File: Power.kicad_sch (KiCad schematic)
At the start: 31 parts, among them J1 Conn_01x02, J6 Conn_01x02, U1 NPM1300-QEAA-R7, U2 TPS76201

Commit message: VSET1 & Ref1 updated
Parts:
- R1: value 270K -> 47K
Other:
- note added: "1) CC1 & CC2 not used. So it is connected to Gnd as mentioned in 6.1.3 USB port detection at page 20&21 in Ref.1 2) Battery NTC not used. So it is connected to ground through 10K resistor 3) To make VOUT1 = 1.8V, VSET1 connected to Resistor K as mentioned in "Table 18: Default VOUT1 using an external resistor" at page 47 Ref.1 4) To make VOUT2 = 3.3V, VSET2 connected to Resistor 100K as mentioned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"
- note removed: "1) CC1 & CC2 not used. So it is connected to Gnd as mentioned in 6.1.3 USB port detection at page 20&21 in Ref.1 2) Battery NTC not used. So it is connected to ground through 10K resistor 3) To make VOUT1 = 2.7V, VSET1 connected to Resistor 270K as mentioned in "Table 18: Default VOUT1 using an external resistor" at page 47 Ref.1 4) To make VOUT2 = 3.3V, VSET2 connected to Resistor 100K as mentio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"
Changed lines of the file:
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@@
 			)
 			(justify left)
+			(href "https://download.mikroe.com/documents/datasheets/nPM1300_datasheet.pdf")
 		)
 	)
@@
 		)
 	)
-	(text "1) CC1 & CC2 not used. So it is connected to Gnd as mentioned in 6.1.3 USB port detection at page 20&21 in Ref.1\n\n2) Battery NTC not used. So it is connected to ground through 10K resistor\n\n3) To make VOUT1 = 2.7V, VSET1 connected to Resistor 270K as mentioned in \"Table 18: Default VOUT1 using an external resistor\" at page 47 Ref.1\n\n4) To make VOUT2 = 3.3V, VSET2 connected to Resistor 100K as mentioned in \"Table 19: Default VOUT2 using an external resistor\" at page 47 Ref.1\n"
+	(text "1) CC1 & CC2 not used. So it is connected to Gnd as mentioned in 6.1.3 USB port detection at page 20&21 in Ref.1\n\n2) Battery NTC not used. So it is connected to ground through 10K resistor\n\n3) To make VOUT1 = 1.8V, VSET1 connected to Resistor K as mentioned in \"Table 18: Default VOUT1 using an external resistor\" at page 47 Ref.1\n\n4) To make VOUT2 = 3.3V, VSET2 connected to Resistor 100K as mentioned in \"Table 19: Default VOUT2 using an external resistor\" at page 47 Ref.1\n"
 		(exclude_from_sim no)
 		(at 14.732 161.29 0)
@@
 			)
 		)
-		(property "Value" "270K"
+		(property "Value" "47K"
 			(at 46.99 105.4099 0)
 			(effects

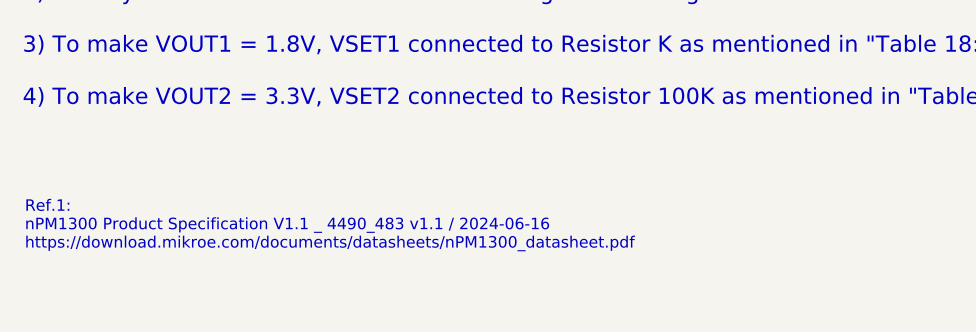
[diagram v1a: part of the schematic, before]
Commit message: Ref link added & Removed charge pumps
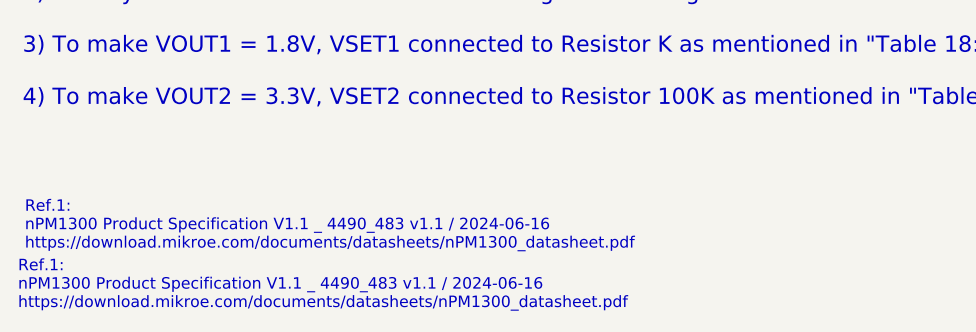
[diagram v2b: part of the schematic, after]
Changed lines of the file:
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@@
 		(comment 2 "K.S.Rangasamy College of Technology")
+	)
+	(text "Ref.1:\nnPM1300 Product Specification V1.1 _ 4490_483 v1.1 / 2024-06-16\nhttps://download.mikroe.com/documents/datasheets/nPM1300_datasheet.pdf"
+		(exclude_from_sim no)
+		(at 14.224 190.754 0)
+		(effects
+			(font
+				(size 1.27 1.27)
+			)
+			(justify left)
+			(href "https://download.mikroe.com/documents/datasheets/nPM1300_datasheet.pdf")
+		)
 	)
 	(text "Power Management IC (PMIC)"

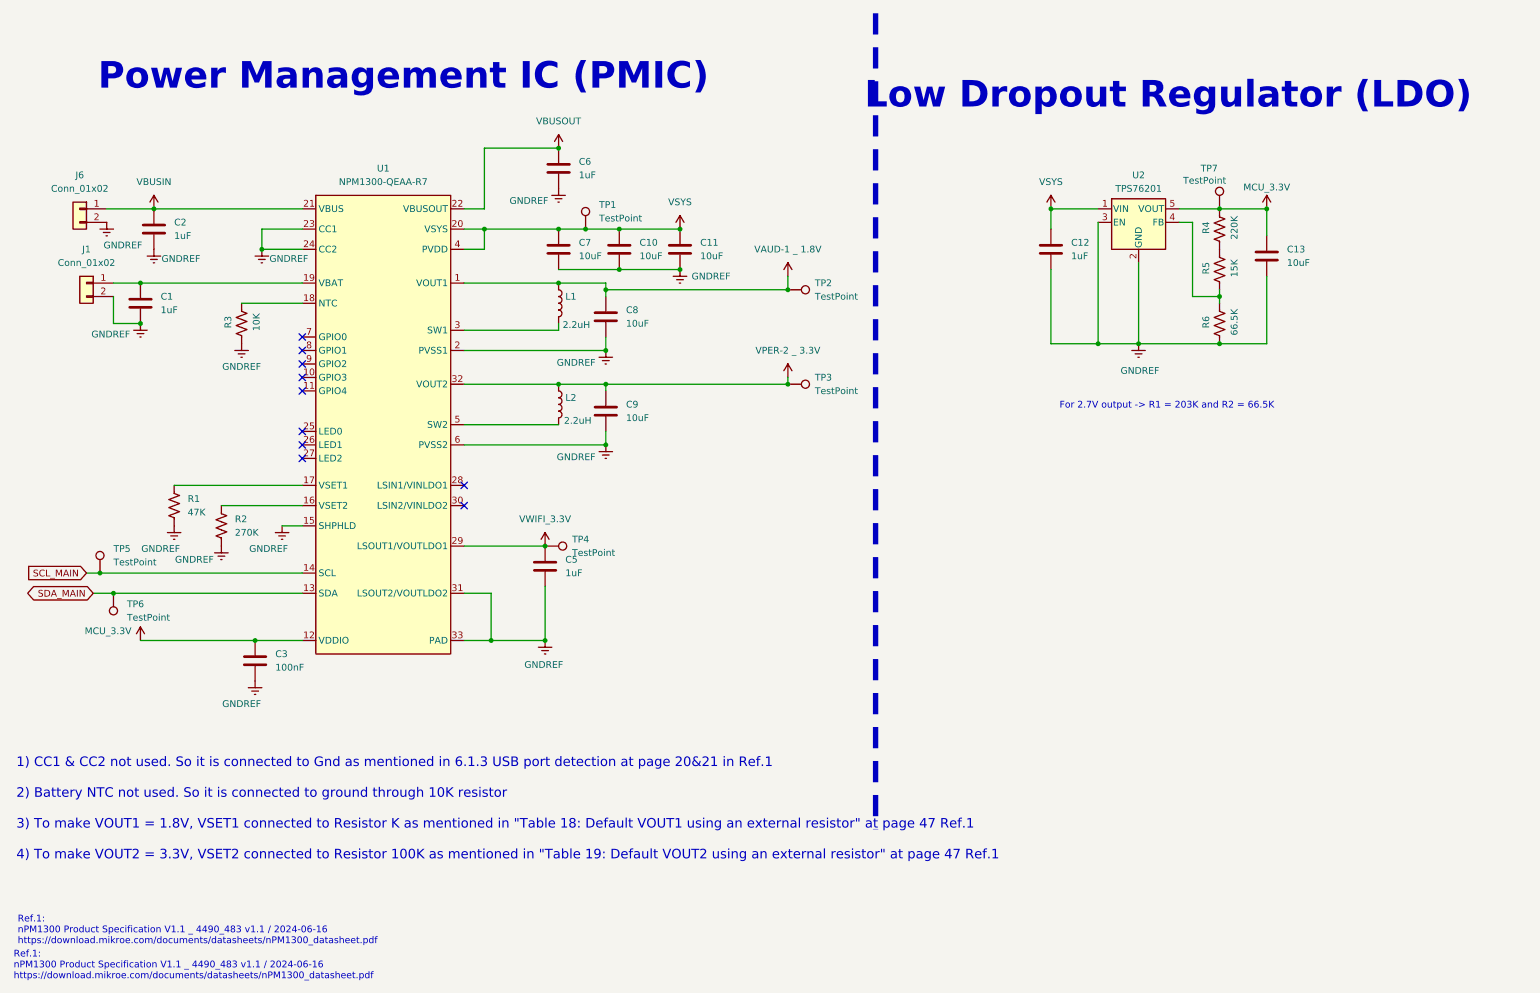
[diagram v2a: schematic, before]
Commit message: LDO feedback resistor updated
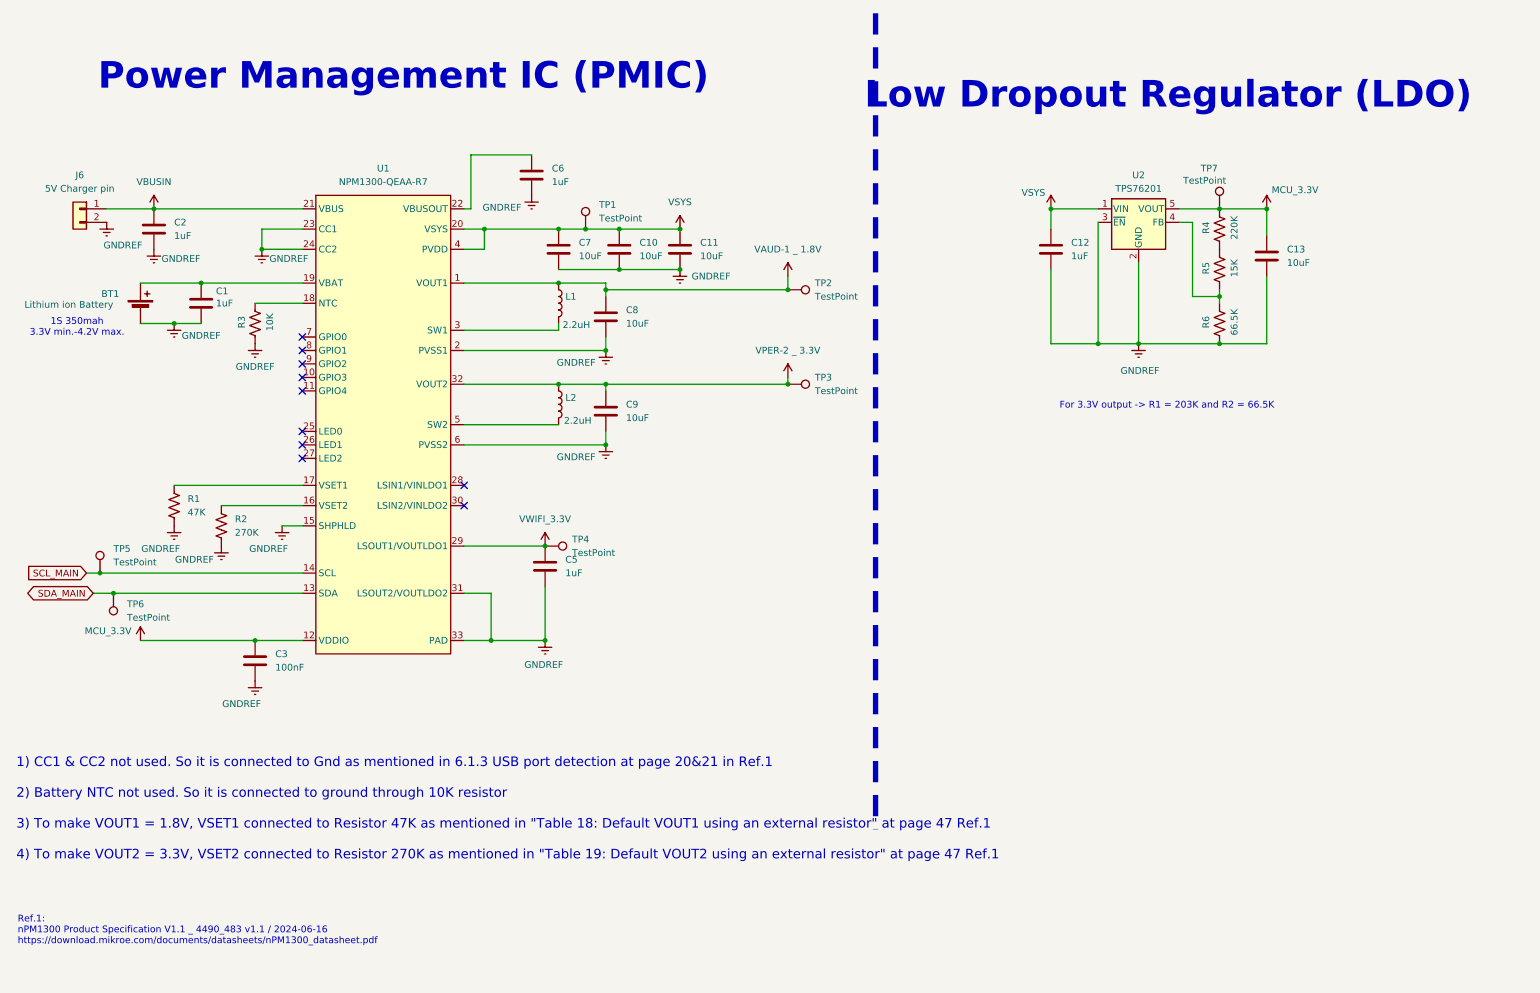
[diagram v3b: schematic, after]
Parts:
- removed J1: Conn_01x02, Custom_Libs:2P_P1mm, symbol Connector_Generic:Conn_01x02
- added BT1: Lithium ion Battery, symbol Device:Battery_Cell
- J6: value Conn_01x02 -> 5V Charger pin
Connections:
- net GNDREF: now also BT1.2 (-)
- net at C1.1, U1.19 (VBAT): now also BT1.1 (+)
- net VBUSOUT: no longer names the net of C6.1, U1.22 (VBUSOUT)
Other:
- note added: "1) CC1 & CC2 not used. So it is connected to Gnd as mentioned in 6.1.3 USB port detection at page 20&21 in Ref.1 2) Battery NTC not used. So it is connected to ground through 10K resistor 3) To make VOUT1 = 1.8V, VSET1 connected to Resistor 47K as mentioned in "Table 18: Default VOUT1 using an external resistor" at page 47 Ref.1 4) To make VOUT2 = 3.3V, VSET2 connected to Resistor 270K as mention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"
- note added: "1S 350mah 3.3V min.-4.2V max."
- note added: "For 3.3V output -> R1 = 203K and R2 = 66.5K"
- note removed: "1) CC1 & CC2 not used. So it is connected to Gnd as mentioned in 6.1.3 USB port detection at page 20&21 in Ref.1 2) Battery NTC not used. So it is connected to ground through 10K resistor 3) To make VOUT1 = 1.8V, VSET1 connected to Resistor K as mentioned in "Table 18: Default VOUT1 using an external resistor" at page 47 Ref.1 4) To make VOUT2 = 3.3V, VSET2 connected to Resistor 100K as mentioned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"
- note removed: "For 2.7V output -> R1 = 203K and R2 = 66.5K"
- moved on the sheet: C1, C6, R3

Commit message: updated version
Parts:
- R5: value 15K -> 26.1K
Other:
- note added: "For 3.3V output -> R1 = 246.1K (220K+26.1K) and R2 = 66.5K"
- note removed: "For 3.3V output -> R1 = 203K and R2 = 66.5K"
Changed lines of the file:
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@@
 		)
 	)
-	(text "For 3.3V output -> R1 = 203K and R2 = 66.5K"
+	(text "For 3.3V output -> R1 = 246.1K (220K+26.1K) and R2 = 66.5K"
 		(exclude_from_sim no)
-		(at 231.394 85.344 0)
+		(at 231.394 84.582 0)
 		(effects
 			(font
@@
 			)
 		)
-		(property "Value" "15K"
+		(property "Value" "26.1K"
 			(at 244.094 59.436 90)
 			(show_name no)
